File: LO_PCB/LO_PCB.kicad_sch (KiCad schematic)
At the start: 90 parts, among them J1 PWR, J2 LO_OUT_A, J3 LO_OUT_B, J4 OSCinP, J5 Conn_01x08, Q1 AO3401A, U1 TPS7A9101DSKT, U2 LMX2582RHAR

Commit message: LO board v1 layout finished
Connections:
- net GND: now also U1.5 (PG)
- net at R31.1: now also R29.1, U2.24 (CSB); no longer U2.17 (SDI)
- net at R32.1: now also U2.17 (SDI); no longer U2.16 (SCK)
- net at U2.20 (MUXOUT): now also R30.1; no longer R33.1
- new net: R33.1, U2.16 (SCK)
- no-connect marks 5 -> 4
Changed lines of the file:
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@@
 	)
 	(junction
+		(at 234.95 217.17)
+		(diameter 0)
+		(color 0 0 0 0)
+	)
+	(junction
 		(at 261.62 132.08)
 		(diameter 0)
@@
 	)
 	(junction
-		(at 232.41 214.63)
-		(diameter 0)
-		(color 0 0 0 0)
-	)
-	(junction
 		(at 137.16 127)
 		(diameter 0)
@@
 	)
 	(no_connect
-		(at 135.89 64.77)
-	)
-	(no_connect
 		(at 251.46 158.75)
 	)
@@
 	(wire
 		(pts
+			(xy 259.08 222.25) (xy 228.6 222.25)
+		)
+		(stroke
+			(width 0)
+			(type default)
+		)
+	)
+	(wire
+		(pts
 			(xy 309.88 85.09) (xy 334.01 85.09)
 		)
@@
 	(wire
 		(pts
-			(xy 167.64 60.96) (xy 160.02 60.96)
+			(xy 228.6 207.01) (xy 234.95 207.01)
 		)
 		(stroke
@@
 	(wire
 		(pts
-			(xy 232.41 207.01) (xy 228.6 207.01)
+			(xy 167.64 60.96) (xy 160.02 60.96)
 		)
 		(stroke
@@
 	(wire
 		(pts
-			(xy 256.54 176.53) (xy 256.54 217.17)
+			(xy 256.54 176.53) (xy 256.54 219.71)
 		)
 		(stroke
@@
 	(wire
 		(pts
-			(xy 232.41 207.01) (xy 232.41 214.63)
+			(xy 160.02 111.76) (xy 160.02 109.22)
 		)
 		(stroke
@@
 	(wire
 		(pts
-			(xy 160.02 111.76) (xy 160.02 109.22)
+			(xy 39.37 91.44) (xy 39.37 97.79)
 		)
 		(stroke
@@
 	(wire
 		(pts
-			(xy 39.37 91.44) (xy 39.37 97.79)
+			(xy 137.16 127) (xy 179.07 127)
 		)
 		(stroke
@@
 	(wire
 		(pts
-			(xy 137.16 127) (xy 179.07 127)
+			(xy 297.18 63.5) (xy 299.72 63.5)
 		)
 		(stroke
@@
 	(wire
 		(pts
-			(xy 297.18 63.5) (xy 299.72 63.5)
+			(xy 309.88 74.93) (xy 309.88 76.2)
 		)
 		(stroke
@@
 	(wire
 		(pts
-			(xy 309.88 74.93) (xy 309.88 76.2)
+			(xy 252.73 179.07) (xy 251.46 179.07)
 		)
 		(stroke
@@
 	(wire
 		(pts
+			(xy 228.6 217.17) (xy 234.95 217.17)
+		)
+		(stroke
+			(width 0)
+			(type default)
+		)
+	)
+	(wire
+		(pts
 			(xy 288.29 163.83) (xy 283.21 163.83)
 		)
@@
 	(wire
 		(pts
-			(xy 261.62 222.25) (xy 228.6 222.25)
+			(xy 228.6 214.63) (xy 261.62 214.63)
 		)
 		(stroke
@@
 	(wire
 		(pts
-			(xy 259.08 219.71) (xy 228.6 219.71)
-		)
-		(stroke
-			(width 0)
-			(type default)
-		)
-	)
-	(wire
-		(pts
 			(xy 182.88 156.21) (xy 190.5 156.21)
 		)
@@
 	(wire
 		(pts
-			(xy 251.46 179.07) (xy 254 179.07)
+			(xy 252.73 177.8) (xy 254 177.8)
 		)
 		(stroke
@@
 	(wire
 		(pts
-			(xy 254 179.07) (xy 254 214.63)
-		)
-		(stroke
-			(width 0)
-			(type default)
-		)
-	)
-	(wire
-		(pts
 			(xy 190.5 179.07) (xy 190.5 194.31)
 		)
@@
 	(wire
 		(pts
-			(xy 232.41 214.63) (xy 228.6 214.63)
-		)
-		(stroke
-			(width 0)
-			(type default)
-		)
-	)
-	(wire
-		(pts
 			(xy 114.3 109.22) (xy 114.3 111.76)
 		)
@@
 	(wire
 		(pts
+			(xy 234.95 207.01) (xy 234.95 217.17)
+		)
+		(stroke
+			(width 0)
+			(type default)
+		)
+	)
+	(wire
+		(pts
 			(xy 175.26 138.43) (xy 175.26 129.54)
 		)
@@
 	(wire
 		(pts
+			(xy 256.54 219.71) (xy 228.6 219.71)
+		)
+		(stroke
+			(width 0)
+			(type default)
+		)
+	)
+	(wire
+		(pts
 			(xy 251.46 173.99) (xy 259.08 173.99)
 		)
@@
 	(wire
 		(pts
+			(xy 234.95 217.17) (xy 254 217.17)
+		)
+		(stroke
+			(width 0)
+			(type default)
+		)
+	)
+	(wire
+		(pts
 			(xy 246.38 101.6) (xy 246.38 102.87)
 		)
@@
 	(wire
 		(pts
-			(xy 259.08 173.99) (xy 259.08 219.71)
-		)
-		(stroke
-			(width 0)
-			(type default)
-		)
-	)
-	(wire
-		(pts
 			(xy 293.37 140.97) (xy 293.37 144.78)
 		)
@@
 	(wire
 		(pts
-			(xy 261.62 168.91) (xy 261.62 222.25)
+			(xy 261.62 168.91) (xy 261.62 214.63)
 		)
 		(stroke
@@
 	(wire
 		(pts
+			(xy 135.89 64.77) (xy 135.89 71.12)
+		)
+		(stroke
+			(width 0)
+			(type default)
+		)
+	)
+	(wire
+		(pts
 			(xy 350.52 63.5) (xy 351.79 63.5)
 		)
@@
 	(wire
 		(pts
+			(xy 252.73 177.8) (xy 252.73 179.07)
+		)
+		(stroke
+			(width 0)
+			(type default)
+		)
+	)
+	(wire
+		(pts
 			(xy 140.97 50.8) (xy 140.97 52.07)
 		)
@@
 	(wire
 		(pts
-			(xy 256.54 217.17) (xy 228.6 217.17)
+			(xy 97.79 170.18) (xy 106.68 170.18)
 		)
 		(stroke
@@
 	(wire
 		(pts
-			(xy 97.79 170.18) (xy 106.68 170.18)
+			(xy 182.88 148.59) (xy 190.5 148.59)
 		)
 		(stroke
@@
 	(wire
 		(pts
-			(xy 182.88 148.59) (xy 190.5 148.59)
+			(xy 114.3 91.44) (xy 190.5 91.44)
 		)
 		(stroke
@@
 	(wire
 		(pts
-			(xy 114.3 91.44) (xy 190.5 91.44)
+			(xy 347.98 137.16) (xy 347.98 138.43)
 		)
 		(stroke
@@
 	(wire
 		(pts
-			(xy 347.98 137.16) (xy 347.98 138.43)
+			(xy 154.94 160.02) (xy 168.91 160.02)
 		)
 		(stroke
@@
 	(wire
 		(pts
-			(xy 254 214.63) (xy 232.41 214.63)
+			(xy 48.26 91.44) (xy 50.8 91.44)
 		)
 		(stroke
@@
 	(wire
 		(pts
-			(xy 154.94 160.02) (xy 168.91 160.02)
+			(xy 254 177.8) (xy 254 217.17)
 		)
 		(stroke
@@
 	(wire
 		(pts
-			(xy 48.26 91.44) (xy 50.8 91.44)
+			(xy 85.09 101.6) (xy 90.17 101.6)
 		)
 		(stroke
@@
 	(wire
 		(pts
-			(xy 85.09 101.6) (xy 90.17 101.6)
+			(xy 97.79 208.28) (xy 97.79 210.82)
 		)
 		(stroke
@@
 	(wire
 		(pts
-			(xy 97.79 208.28) (xy 97.79 210.82)
+			(xy 39.37 88.9) (xy 39.37 91.44)
 		)
 		(stroke
@@
 	(wire
 		(pts
-			(xy 39.37 88.9) (xy 39.37 91.44)
+			(xy 259.08 173.99) (xy 259.08 222.25)
 		)
 		(stroke
@@
 					(unit 1)
 				)
+			)
+		)
+	)
+	(symbol
+		(lib_id "power:GND")
+		(at 135.89 71.12 0)
+		(unit 1)
+		(body_style 1)
+		(exclude_from_sim no)
+		(in_bom yes)
+		(on_board yes)
+		(in_pos_files yes)
+		(dnp no)
+		(fields_autoplaced yes)
+		(property "Reference" "#PWR043"
+			(at 135.89 77.47 0)
+			(hide yes)
+			(show_name no)
+			(do_not_autoplace no)
+			(effects
+				(font
+					(size 1.27 1.27)
+				)
+			)
+		)
+		(property "Value" "GND"
+			(at 135.89 76.2 0)
+			(show_name no)
+			(do_not_autoplace no)
+			(effects
+				(font
+					(size 1.27 1.27)
+				)
+			)
+		)
+		(property "Footprint" ""
+			(at 135.89 71.12 0)
+			(hide yes)
+			(show_name no)
+			(do_not_autoplace no)
+			(effects
+				(font
+					(size 1.27 1.27)
+				)
+			)
+		)
+		(property "Datasheet" ""
+			(at 135.89 71.12 0)
+			(hide yes)
+			(show_name no)
+			(do_not_autoplace no)
+			(effects
+				(font
+					(size 1.27 1.27)
+				)
+			)
+		)
+		(property "Description" "Power symbol creates a global label with name \"GND\" , ground"
+			(at 135.89 71.12 0)
+			(hide yes)
+			(show_name no)
+			(do_not_autoplace no)
+			(effects
+				(font
+					(size 1.27 1.27)
+				)
+			)
+		)
+		(pin "1"
+		)
+		(instances
+			(project "LO_PCB"
+				(path "/820b88fc-e97a-437b-924c-526a252f36ed"
+					(reference "#PWR043")
+					(unit 1)
+				)

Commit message: stuff and added nice border
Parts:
- removed J5: Conn_01x08, Connector_PinHeader_2.54mm:PinHeader_1x08_P2.54mm_Vertical, symbol Connector_Generic:Conn_01x08
- added C44: 10uF, Capacitor_SMD:C_0603_1608Metric, symbol Device:C
- added H1, H2, H3, H4: MountingHole_Pad, MountingHole:MountingHole_2.2mm_M2_Pad_Via, symbol Mechanical:MountingHole_Pad
- added J2: Conn_01x06, Connector_PinHeader_2.54mm:PinHeader_1x06_P2.54mm_Vertical, symbol Connector_Generic:Conn_01x06
- C43: renamed from C42; value 1uF -> 0.1uF
- R22: value 10 -> 1
- R23: value 68 -> 47
- R24: value 68 -> 18
- renumbered C43 to C42, C44 to C45, C45 to C46, C46 to C47, J2 to LO_OUT_A1, J3 to LO_OUT_B1, J4 to OSCIn1
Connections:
- net GND: now also C44.2, H1.1, H2.1, H3.1, H4.1, J2.6 (Pin_6)
- net INT_OSC_ENABLE: now also J2.1 (Pin_1)
- net at R31.2: now also J2.4 (Pin_4)
- net at R30.2: now also J2.5 (Pin_5)
- net at R33.2: now also J2.2 (Pin_2)
- net at R32.2: now also J2.3 (Pin_3)
- net at C43.1, R22.2, XTAL1.4 (VCC): now also C44.1
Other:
- moved on the sheet: C43

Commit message: small update and plan for upgrade of frequence reference XO
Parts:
- C1, C13, C15, C22, C24, C43, C5: MPN (none) -> GRM188R71H104KA93D; Manufacturer (none) -> Murata
- C10, C8: MPN (none) -> GJM1555C1H3R9BB01D; Manufacturer (none) -> Murata
- C11, C33, C38, C41: MPN (none) -> GRM188R71C105KA12D; Manufacturer (none) -> Murata
- C12, C18, C20, C26, C32, C6, C7: MPN (none) -> GRM1555C1H101JA01D; Manufacturer (none) -> Murata
- C14, C16, C2, C23, C25, C36, C39, C4, C40, C42: MPN (none) -> GRM188R61A106KAALD; Manufacturer (none) -> Murata
- C17, C19, C3: MPN (none) -> GRM155R71H103KA88D; Manufacturer (none) -> Murata
- C21, C27, C28, C29, C30, C31, C45, C46, C47: MPN (none) -> GRM155R71H104KE14D; Manufacturer (none) -> Murata
- C34: MPN (none) -> GRM1885C1H332JA01D; Manufacturer (none) -> Murata
- C35: MPN (none) -> GRM21BR71E684KA88L; Manufacturer (none) -> Murata
- C37: MPN (none) -> GRM1885C1H122JA01D; Manufacturer (none) -> Murata
- C44: Dielectric X7R -> X5R; MPN (none) -> GRM188R61A106KAALD; Manufacturer (none) -> Murata
- C9: MPN (none) -> GJM1555C1H6R8BB01D; Manufacturer (none) -> Murata
- L1, L2: MPN (none) -> 0402DC-11NXGRW; Manufacturer (none) -> Coilcraft
- LO_OUT_A1, LO_OUT_B1, OSCIn1: MPN (none) -> 60312202114513; Manufacturer (none) -> Wurth Elektronik
- Q1: MPN (none) -> AO3401A; Manufacturer (none) -> Alpha & Omega Semiconductor
- R1: MPN (none) -> RG1005P-3161-B-T5; Manufacturer (none) -> Susumu
- R10, R11, R12, R13: MPN (none) -> RG1005P-49R9-B-T5; Manufacturer (none) -> Susumu
- R14, R15, R17, R18: MPN (none) -> RG1005P-101-B-T5; Manufacturer (none) -> Susumu
- R16: MPN (none) -> RC0603FR-0712RL; Manufacturer (none) -> Yageo
- R19, R21, R29: MPN (none) -> RC0603FR-0710KL; Manufacturer (none) -> Yageo
- R2: MPN (none) -> RC0603FR-07100KL; Manufacturer (none) -> Yageo
- R20, R30, R31, R32, R33: MPN (none) -> RC0603JR-0733RL; Manufacturer (none) -> Yageo
- R22: MPN (none) -> RC0603FR-071RL; Manufacturer (none) -> Yageo
- R23: MPN (none) -> RG1005P-470-B-T5; Manufacturer (none) -> Susumu
- R24, R25, R26: MPN (none) -> RG1005P-180-B-T5; Manufacturer (none) -> Susumu
- R27, R28: MPN (none) -> RG1005P-680-B-T5; Manufacturer (none) -> Susumu
- R3: MPN (none) -> RG1005P-102-B-T5; Manufacturer (none) -> Susumu
- R4, R5: MPN (none) -> RC0603JR-070RL; Manufacturer (none) -> Yageo
- R6, R7, R8, R9: MPN (none) -> RC0402JR-070RL; Manufacturer (none) -> Yageo
- U1: MPN (none) -> TPS7A9101DSKT; Manufacturer (none) -> Texas Instruments
- U2: MPN (none) -> LMX2582RHAR; Manufacturer (none) -> Texas Instruments
- XTAL1: value CWX813-100.0M -> TB612-100.0M; MPN (none) -> TB612-100.0M; Manufacturer (none) -> Connor-Winfield
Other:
- note added: "*** XTAL1 WILL BE CHANGED WITH TB612-100.0M - 10-PAD TCXO *** Symbol and footprint are STILL the 4-pad CWX813 and MUST be redrawn before fab. TB612 pads: 4=GND 5=OUTPUT 8=ENABLE 9=Vcc 10=NC (TCXO) 1,2,3,6,7=DNC (leave floating) Every connection moves: EN 1->8, GND 2->4, OUT 3->5, Vcc 4->9. Also add a 10nF bypass at pad 9, within 2.54 mm. Datasheet: docs/tx380.pdf page 5."
- note added: "On-Board Oscillator 100 MHz TCXO, +/-0.5 ppm"
- note removed: "On-Board Oscillator 100 MHz, 25ppm"

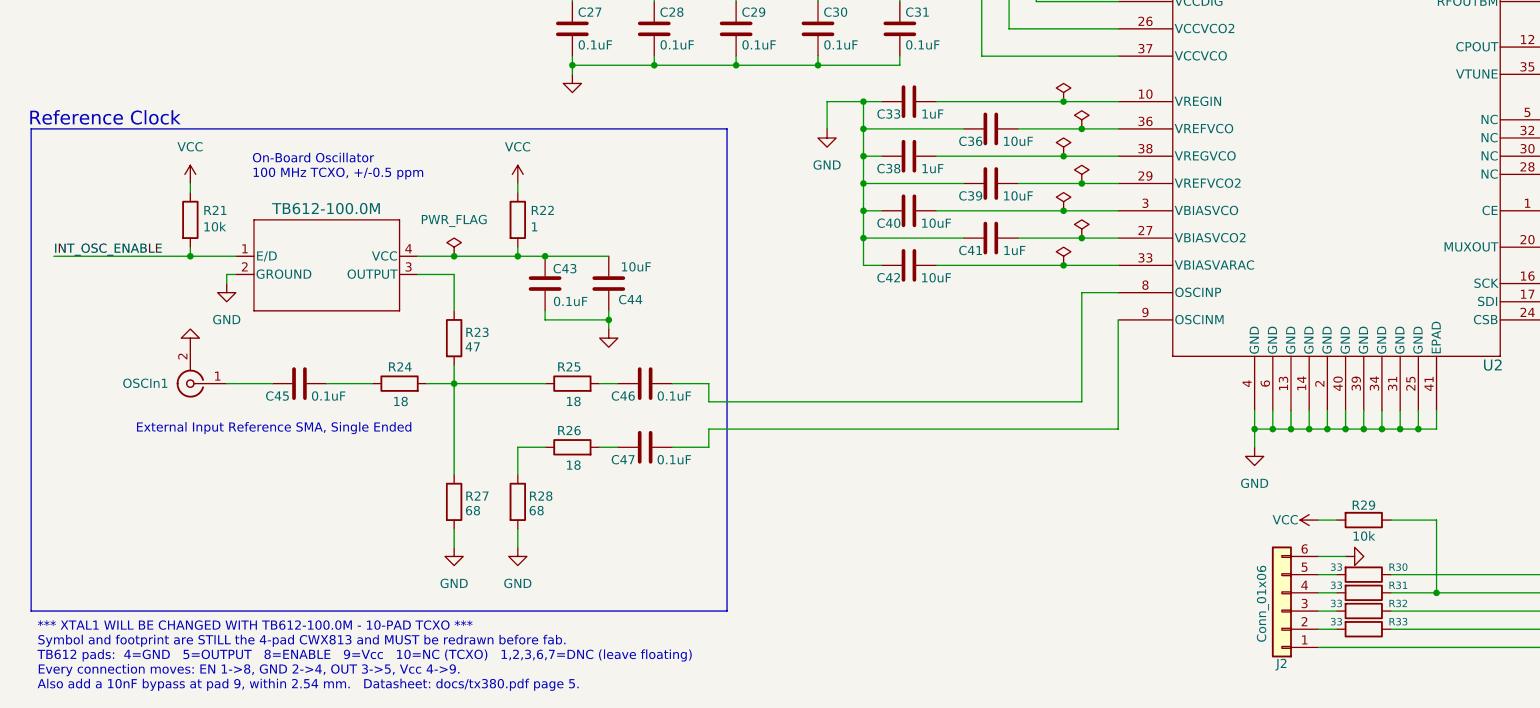
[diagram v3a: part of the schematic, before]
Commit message: changed reference oscillator to TB612-100.0M for better frequency stability and phase noise
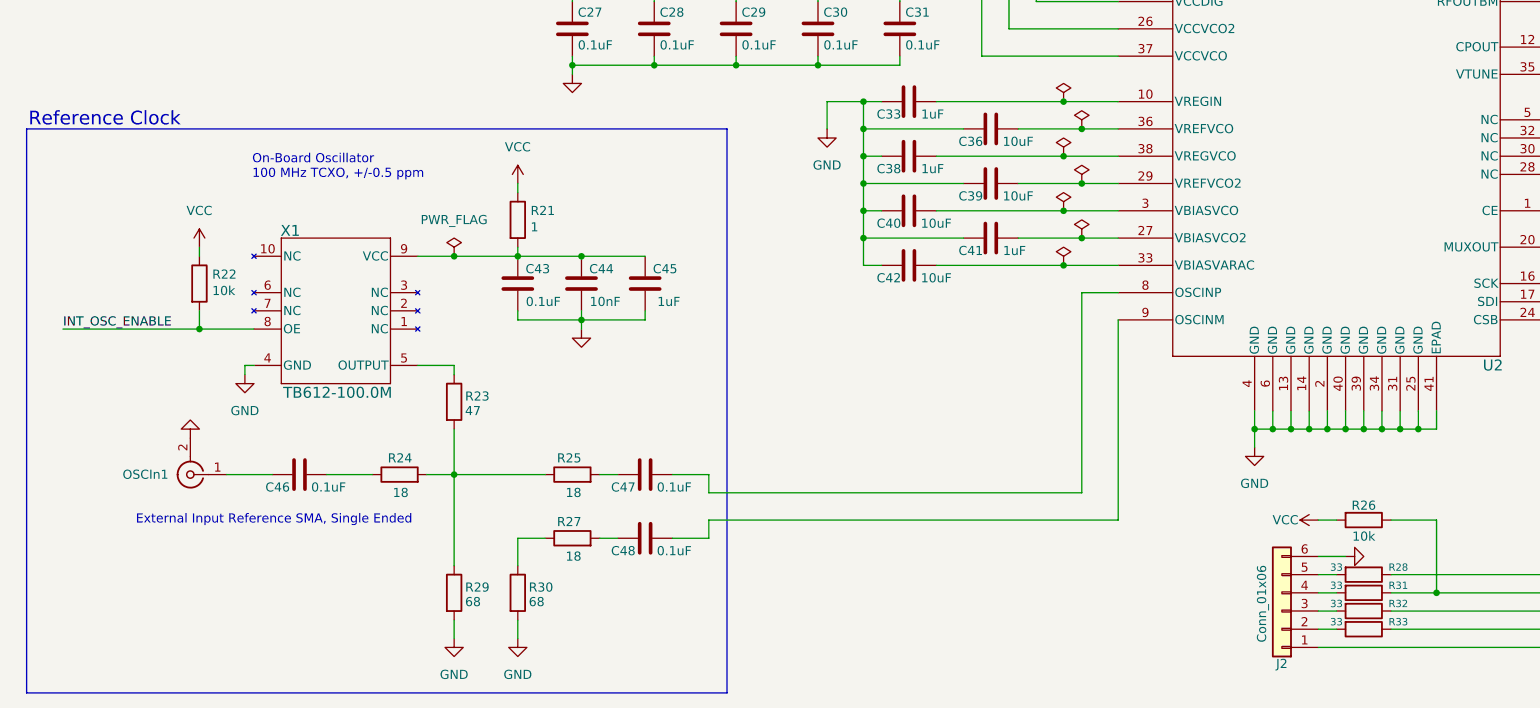
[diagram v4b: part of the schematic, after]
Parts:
- removed XTAL1: TB612-100.0M, Snapeda:CWX813-100.0M_CNW-L, symbol Snapeda:CWX813-100.0M
- added C45: 1uF, Capacitor_SMD:C_0603_1608Metric, symbol Device:C
- added X1: TB612-100.0M, Snapeda:TB612_CNW, symbol Snapeda:TB612-100.0M
- C44: value 10uF -> 10nF; Dielectric X5R -> X7R; MPN GRM188R61A106KAALD -> (none); Manufacturer Murata -> (none); Tolerance +/-10% -> (none); Voltage 25V -> (none)
- renumbered C45 to C46, C46 to C47, C47 to C48, R22 to R21, R21 to R22, R29 to R26, R26 to R27, R30 to R28, R27 to R29, R28 to R30
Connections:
- net GND: now also C45.2, X1.4 (GND)
- net INT_OSC_ENABLE: now also X1.8 (OE)
- net at C43.1, C44.1, R21.2: now also C45.1, X1.9 (VCC)
- net at R23.1: now also X1.5 (OUTPUT)
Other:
- note removed: "*** XTAL1 WILL BE CHANGED WITH TB612-100.0M - 10-PAD TCXO *** Symbol and footprint are STILL the 4-pad CWX813 and MUST be redrawn before fab. TB612 pads: 4=GND 5=OUTPUT 8=ENABLE 9=Vcc 10=NC (TCXO) 1,2,3,6,7=DNC (leave floating) Every connection moves: EN 1->8, GND 2->4, OUT 3->5, Vcc 4->9. Also add a 10nF bypass at pad 9, within 2.54 mm. Datasheet: docs/tx380.pdf page 5."
- moved on the sheet: C43, C44, C46, C47, C48, OSCIn1, R22, R23, R24, R25, R27, R29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

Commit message: fixed errors and small bugs
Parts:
- renumbered OSCIn1 to EXT_OSC_IN, LO_OUT_A1 to LO_OUT_A, LO_OUT_B1 to LO_OUT_B
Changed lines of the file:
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@@
 		(in_pos_files yes)
 		(dnp no)
-		(property "Reference" "OSCIn1"
+		(property "Reference" "EXT_OSC_IN"
 			(at 57.912 200.66 0)
 			(show_name no)
@@
 			(project "LO_PCB"
 				(path "/820b88fc-e97a-437b-924c-526a252f36ed"
-					(reference "OSCIn1")
+					(reference "EXT_OSC_IN")
 					(unit 1)
 				)
@@
 		(in_pos_files yes)
 		(dnp no)
-		(property "Reference" "LO_OUT_A1"
+		(property "Reference" "LO_OUT_A"
 			(at 360.68 65.0633 0)
 			(show_name no)
@@
 			(project "LO_PCB"
 				(path "/820b88fc-e97a-437b-924c-526a252f36ed"
-					(reference "LO_OUT_A1")
+					(reference "LO_OUT_A")
 					(unit 1)
 				)
@@
 		(in_pos_files yes)
 		(dnp no)
-		(property "Reference" "LO_OUT_B1"
+		(property "Reference" "LO_OUT_B"
 			(at 360.68 86.6533 0)
 			(show_name no)
@@
 			(project "LO_PCB"
 				(path "/820b88fc-e97a-437b-924c-526a252f36ed"
-					(reference "LO_OUT_B1")
+					(reference "LO_OUT_B")
 					(unit 1)
 				)

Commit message: added a tuning parallel cap for ref xo output to better match expected drive. todo: tune resistor values to better suit the TCXO
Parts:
- added C46: 15pF, Capacitor_SMD:C_0402_1005Metric, symbol Device:C
- renumbered C46 to C47, C47 to C48, C48 to C49, EXT_OSC_IN to EXT_OSC_IN1, LO_OUT_A to LO_OUT_A1, LO_OUT_B to LO_OUT_B1
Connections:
- net GND: now also C46.2
- net at R23.1, X1.5 (OUTPUT): now also C46.1
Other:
- moved on the sheet: R23

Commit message: final final LO PCB?
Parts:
- added C50: 0.1uF, Capacitor_SMD:C_0402_1005Metric, symbol Device:C
- C14, C16, C2, C23, C25, C36, C39, C4, C40, C42: Tolerance +/-20% -> +/-10%
- C44: MPN (none) -> GRM188R71H103KA01D; Manufacturer (none) -> Murata; Tolerance (none) -> +/-10%; Voltage (none) -> 50V
- C45: Dielectric X5R -> X7R; MPN (none) -> GRM188R71C105KA12D; Manufacturer (none) -> Murata; Tolerance (none) -> +/-10%; Voltage (none) -> 16V
- EXT_REF_IN1: renamed from EXT_OSC_IN1; value OSCinP -> EXT_REF_IN
- R1, R10, R11, R12, R13, R3: Tolerance +/-1% -> +/-0.1%
- R14, R15, R17, R18: Tolerance (none) -> +/-0.1%
- R19, R2, R21, R22, R26: Tolerance +/-5% -> +/-1%
- R20: Tolerance +/-1% -> +/-5%
- R23, R24, R25, R27: Tolerance +/-5% -> +/-0.1%
- R29: value 68 -> 56; MPN RG1005P-680-B-T5 -> RG1005P-560-B-T5; Tolerance +/-5% -> +/-0.1%
- R30: value 68 -> 36; MPN RG1005P-680-B-T5 -> RG1005P-360-B-T5; Tolerance +/-5% -> +/-0.1%
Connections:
- net at C46.1, X1.5 (OUTPUT): now also C50.2; no longer R23.1
- new net: C50.1, R23.1
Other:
- moved on the sheet: C46, C47, C48, C49, EXT_REF_IN1, R23, R24, R25, R27, R29, R30
